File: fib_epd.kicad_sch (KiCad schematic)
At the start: 56 parts, among them J4 ED060SC4, J5 ED060SC7, U1 TPS651851RSLT, U4 ESP32-S3-WROOM-1U

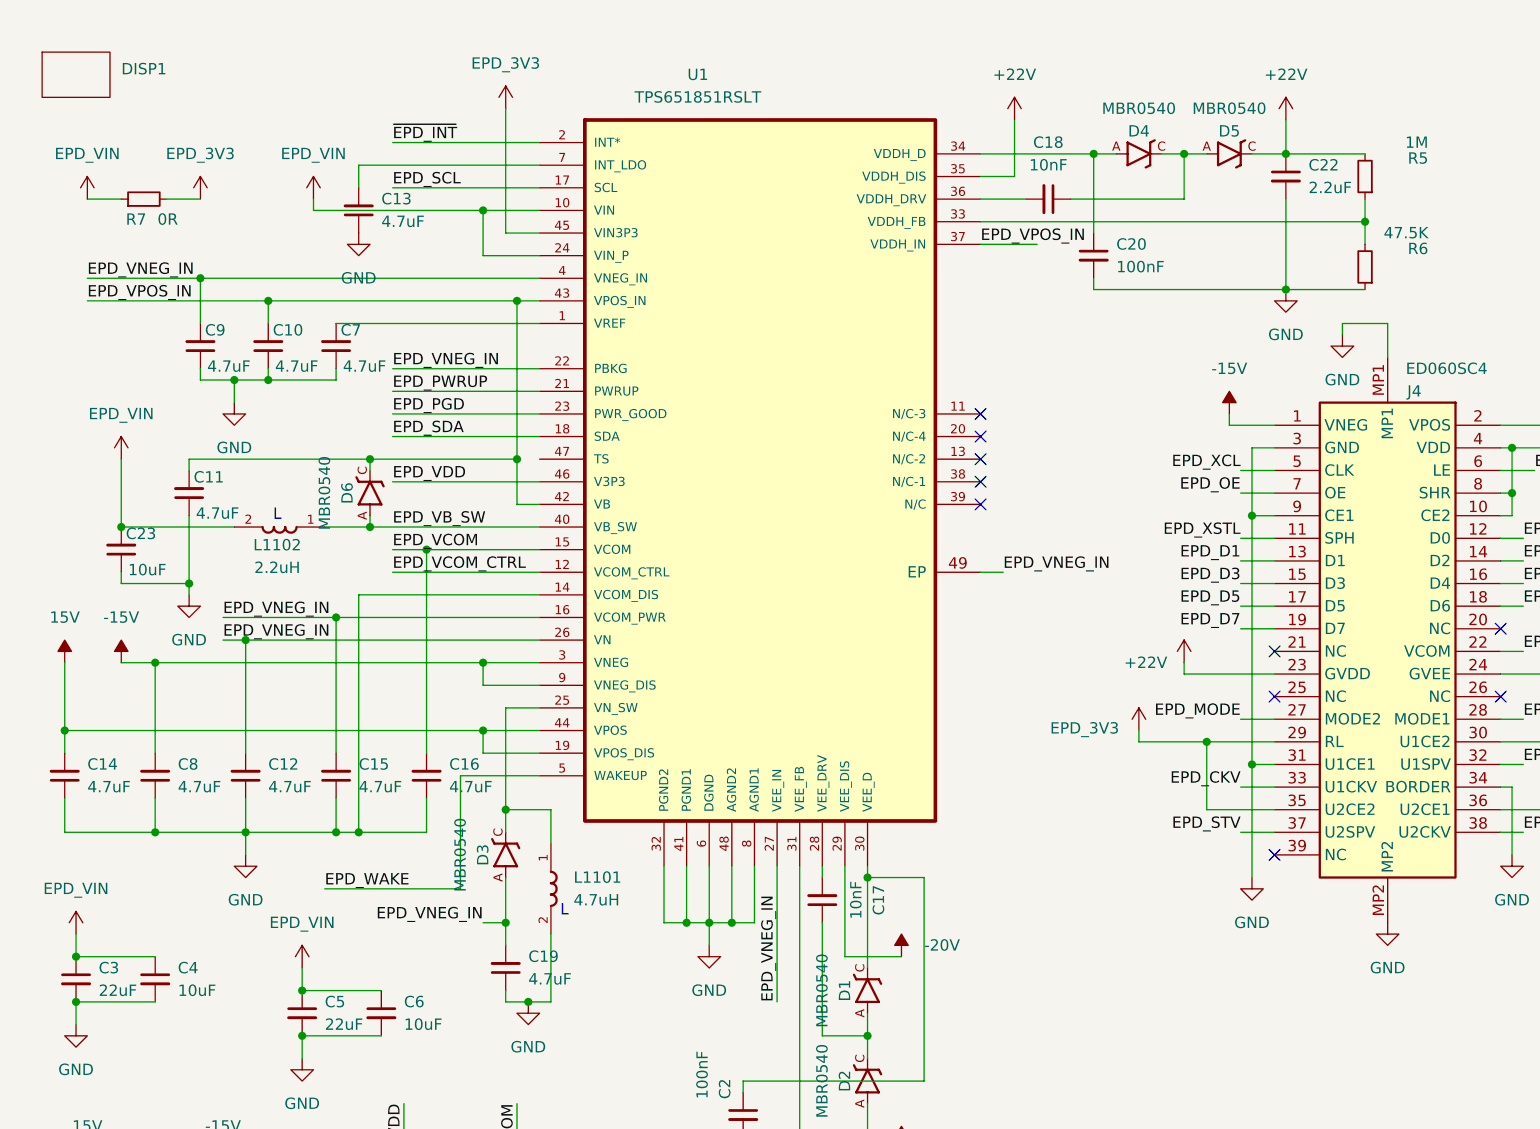
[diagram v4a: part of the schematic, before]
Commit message: adde testpoints, fixed power supplies, ready to order
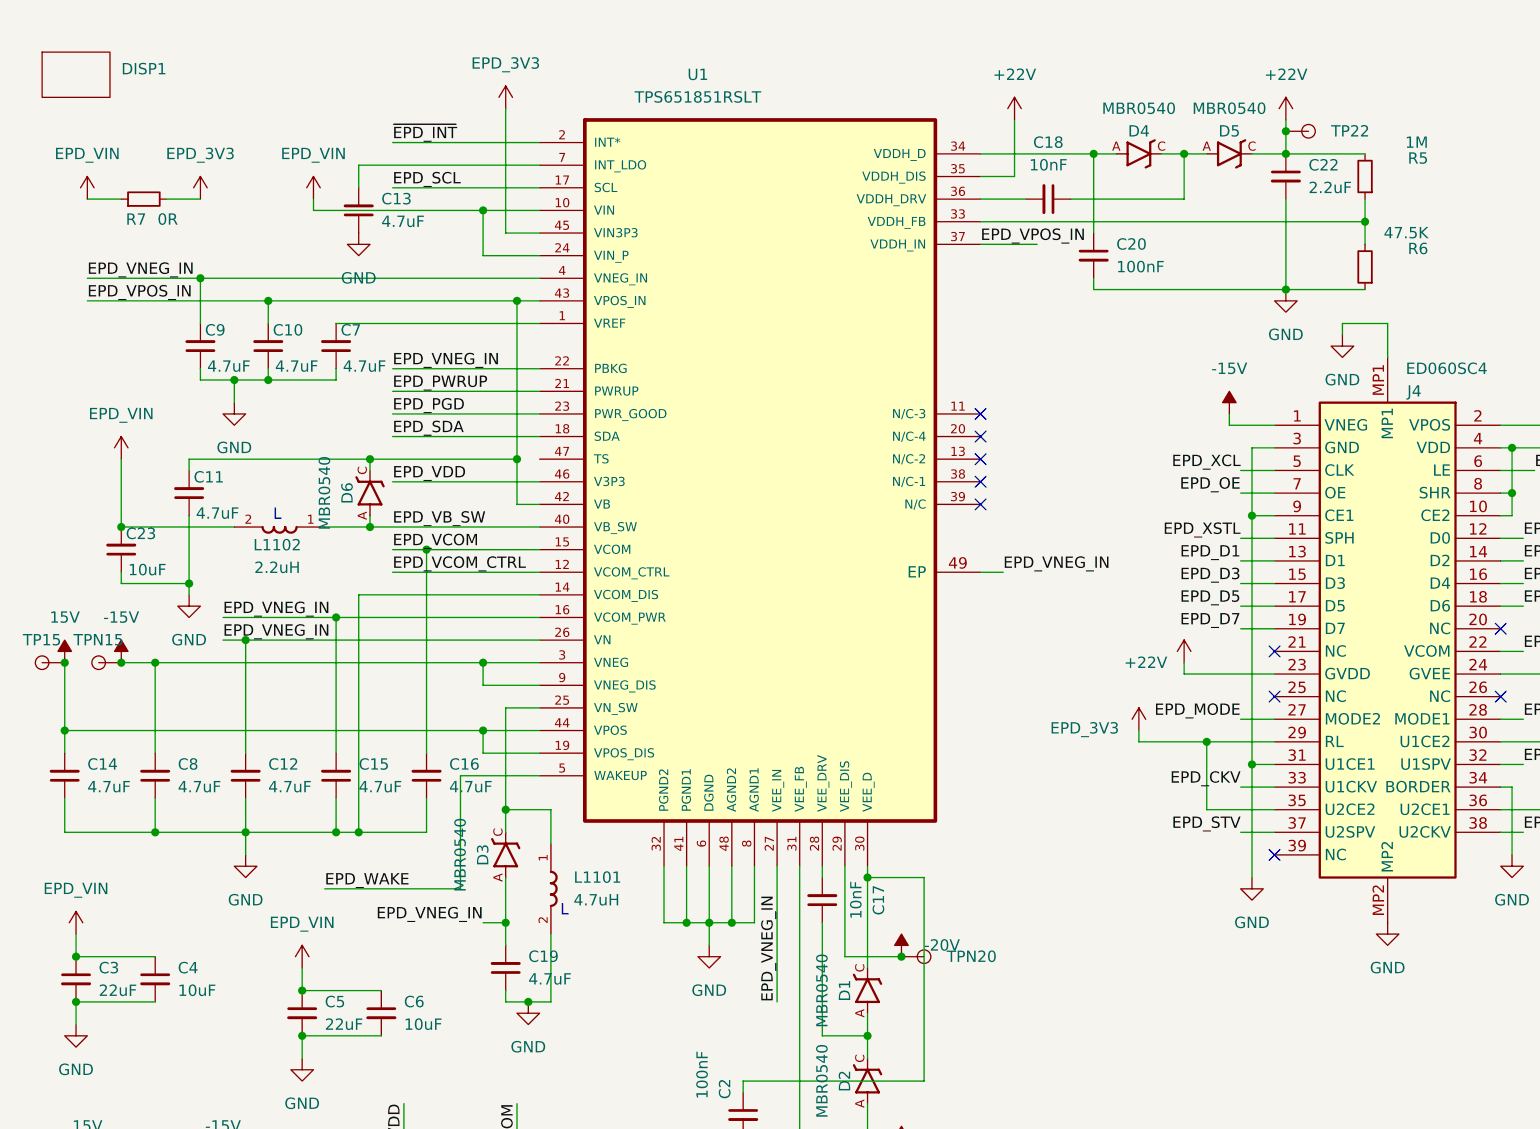
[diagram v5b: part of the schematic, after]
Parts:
- added TP15, TP22, TPN15, TPN20: TestPoint, TestPoint:TestPoint_Pad_D1.0mm, symbol Fibel2:TestPoint
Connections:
- net +22V: now also TP22.1
- net -15V: now also TPN15.1
- net -20V: now also TPN20.1
- net 15V: now also TP15.1
